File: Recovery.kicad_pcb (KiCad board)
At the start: 2 copper layers, 45 x 37.5 mm, 42 parts, among them J1 DE9_Plug, J2 JST-GH, J3 JST-GH, J4 SWD Header, J5 JST-GH, J6 Micro-Fit, J8 Micro-Fit, U1 STM32F042F6P6TR, U2 AZ1117I-3.3, U3 L7805, U4 MCP2562-E-SN, U5 INA350ABSIDSGR, U6 INA350ABSIDSGR, U8 INA350ABSIDSGR, Y1 8M, ?p

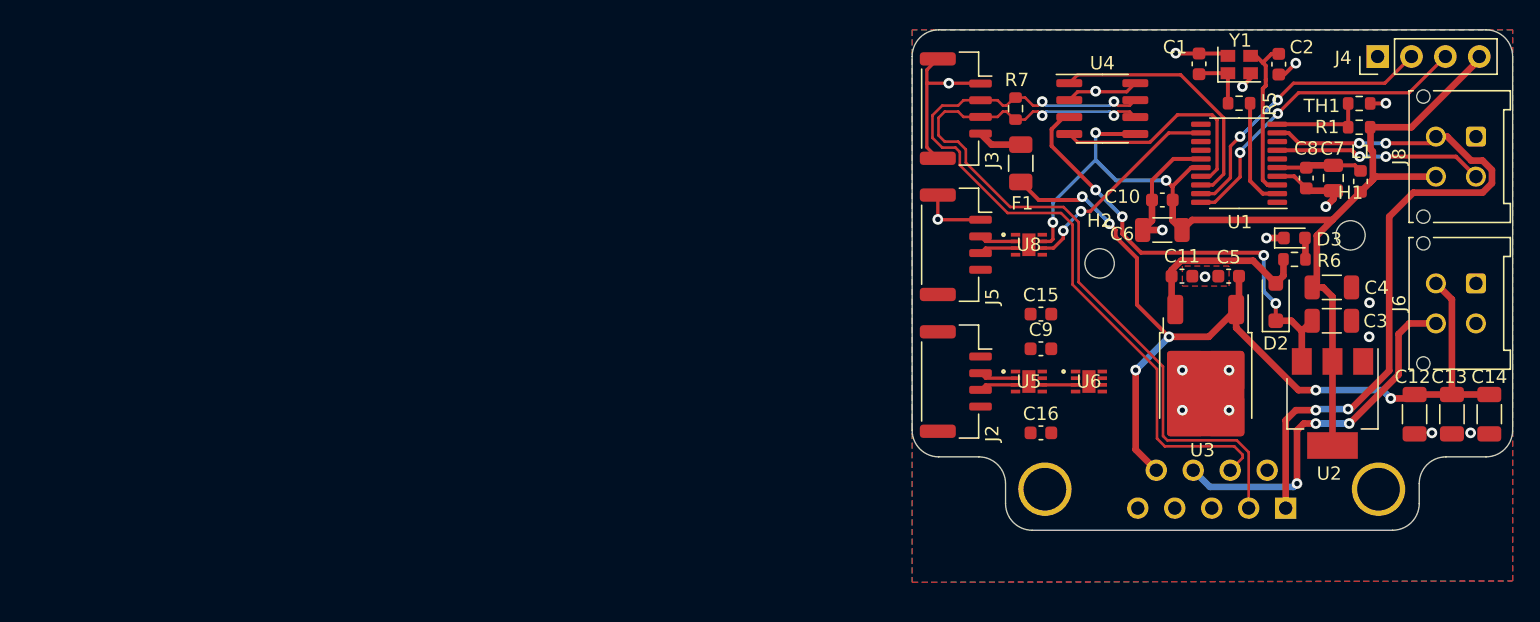
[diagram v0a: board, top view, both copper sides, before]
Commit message: fix pcb size
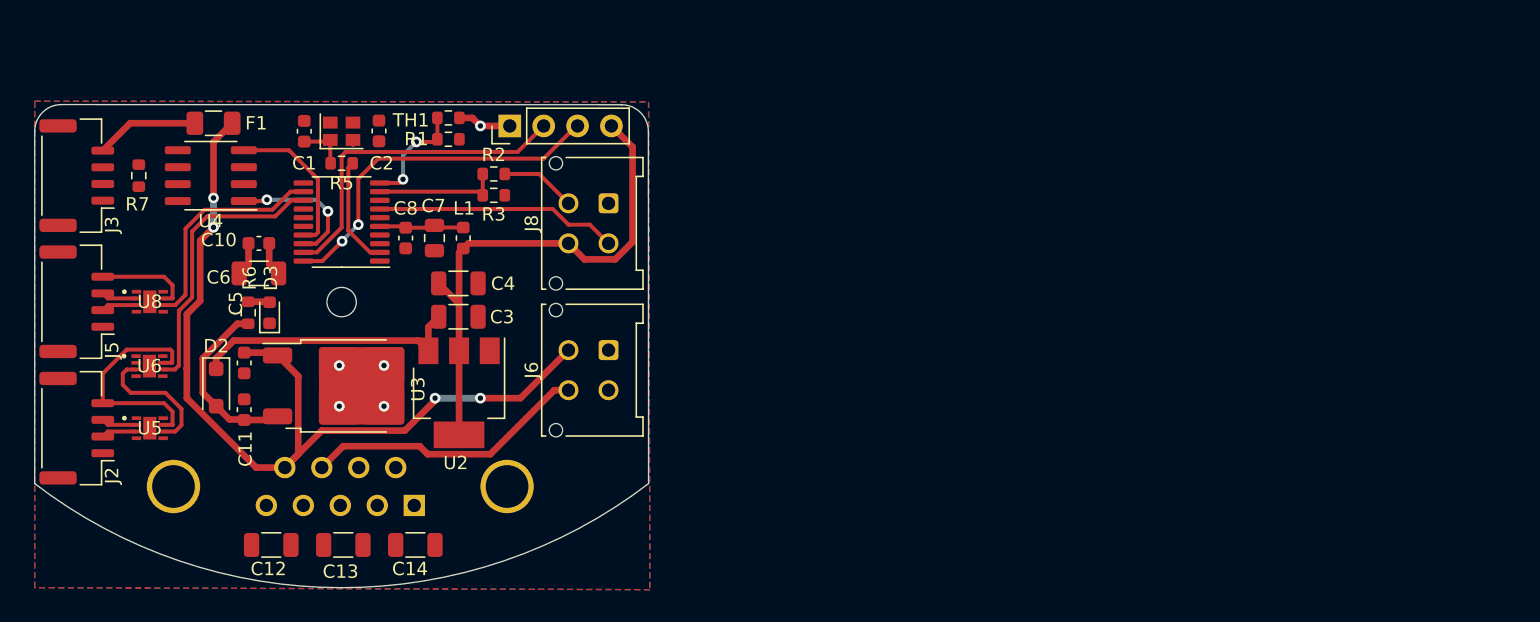
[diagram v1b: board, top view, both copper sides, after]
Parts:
- removed C15, C16, C9: 100n, Capacitor_SMD:C_0603_1608Metric
- removed H2: MountingHole_Pad, MountingHole:MountingHole_2.2mm_M2
- added R2: 1K8, Resistor_SMD:R_0603_1608Metric, F.Cu at (91.4, 86.8)
- added R3: 1K, Resistor_SMD:R_0603_1608Metric, F.Cu at (91.4, 88.4)
- J2, J3, J5: footprint Connector_JST:JST_GH_SM04B-GHS-TB_1x04-1MP_P1.25mm_Horizontal -> Connector_JST:JST_GH_BM04B-GHS-TBT_1x04-1MP_P1.25mm_Vertical
- moved C12 86.2 mm to (74.7, 114.6), turned to 0 degrees
- moved C13 83.7 mm to (80.1, 114.6), turned to 0 degrees
- moved C14 81.1 mm to (85.5, 114.6), turned to 180 degrees
- moved D2 79.7 mm to (70.6, 102.8), turned to -90 degrees
- moved R6 78.5 mm to (73.0, 97.2), turned to 90 degrees
- moved D3 77.0 mm to (74.6, 97.2), turned to 90 degrees
- moved H1 75.8 mm to (80.0, 96.4)
- moved C5 74.1 mm to (72.7, 101.0), turned to 90 degrees
- moved C11 71.0 mm to (72.7, 104.5), turned to -90 degrees
- moved U6 70.4 mm to (65.6, 101.2)
- moved TH1 68.3 mm to (88.0, 82.6)
- moved R1 68.3 mm to (88.0, 84.2)
- moved C10 67.8 mm to (73.8, 92.0)
- moved C6 67.8 mm to (73.8, 94.3)
- moved C8 67.6 mm to (84.8, 91.6)
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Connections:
- U1 pad 9: DEPLOYMENT_SIGNAL -> DEPLOYMENT_PIN
- U5 pad 2: Net-(J2-Pin_2) -> Net-(J2-Pin_3)
- U5 pad 3: Net-(J2-Pin_3) -> Net-(J2-Pin_2)
- U8 pad 2: Net-(J5-Pin_2) -> Net-(J5-Pin_3)
- U8 pad 3: Net-(J5-Pin_3) -> Net-(J5-Pin_2)
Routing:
- net CAN-: track 61.3 -> 0.00 mm, vias 2 -> 0
- net CAN+: track 59.6 -> 0.00 mm, vias 2 -> 0
- net DEPLOYMENT_SIGNAL: track 55.1 -> 5.69 mm, vias 4 -> 0
- net GND: track 48.1 -> 7.44 mm, vias 19 -> 5
- net PRESSURE_SENSOR_1: track 0.00 -> 21.1 mm
- net +3V3: track 80.2 -> 66.2 mm, vias 3 -> 0
- net +5V: track 33.9 -> 20.4 mm, vias 4 -> 0
- net OSC_OUT: track 13.0 -> 0.21 mm
- net DEPLOYMENT_PIN: track 0.00 -> 9.43 mm
- net CAN_TX: track 19.4 -> 10.8 mm, vias 0 -> 2
- net Net-(U5-OUT): track 2.50 -> 9.91 mm
- net +VDC: track 27.9 -> 21.4 mm, vias 3 -> 0
- net CAN_RX: track 17.5 -> 11.6 mm
- net Net-(J3-Pin_4): track 3.36 -> 7.75 mm
- net SWDIO: track 21.5 -> 25.1 mm, vias 2 -> 0
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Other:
- board size 45 x 37.5 mm -> 46 x 36.2 mm

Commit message: finish traces
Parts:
- moved R5 2.86 mm to (77.4, 84.8)
- moved R6 1.41 mm to (74.0, 98.2), turned to 0 degrees
- moved Y1 1.02 mm to (81.0, 83.8)
- moved C2 0.86 mm to (83.6, 83.9)
- moved D3 0.85 mm to (74.0, 96.6), turned to 0 degrees
- moved C1 0.49 mm to (77.4, 83.2), turned to 0 degrees
- moved H1 0.30 mm to (80.0, 96.7)
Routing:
- net +3V3: track 66.2 -> 123.4 mm, vias 0 -> 7
- net CAN-: track 0.00 -> 55.9 mm
- net CAN+: track 0.00 -> 52.1 mm
- net DEPLOYMENT_SIGNAL: track 5.69 -> 40.5 mm, vias 0 -> 1
- net GND: track 7.44 -> 30.0 mm, vias 5 -> 19
- net +5V: track 20.4 -> 38.8 mm, vias 0 -> 2
- net +BATT: track 68.6 -> 86.4 mm, vias 4 -> 6
- net OSC_OUT: track 0.21 -> 11.9 mm
- net CAN_TX: track 10.8 -> 22.0 mm, vias 2 -> 0
- net OSC_IN: track 8.22 -> 10.5 mm
- net Net-(C1-Pad2): track 3.76 -> 4.83 mm
- net TEMPERATURE_SENSOR: track 8.32 -> 7.27 mm, vias 2 -> 0
- net SWCLK: track 26.8 -> 27.7 mm
- net CAN_RX: track 11.6 -> 12.2 mm
- net SWDIO: track 25.1 -> 24.6 mm, vias 0 -> 2

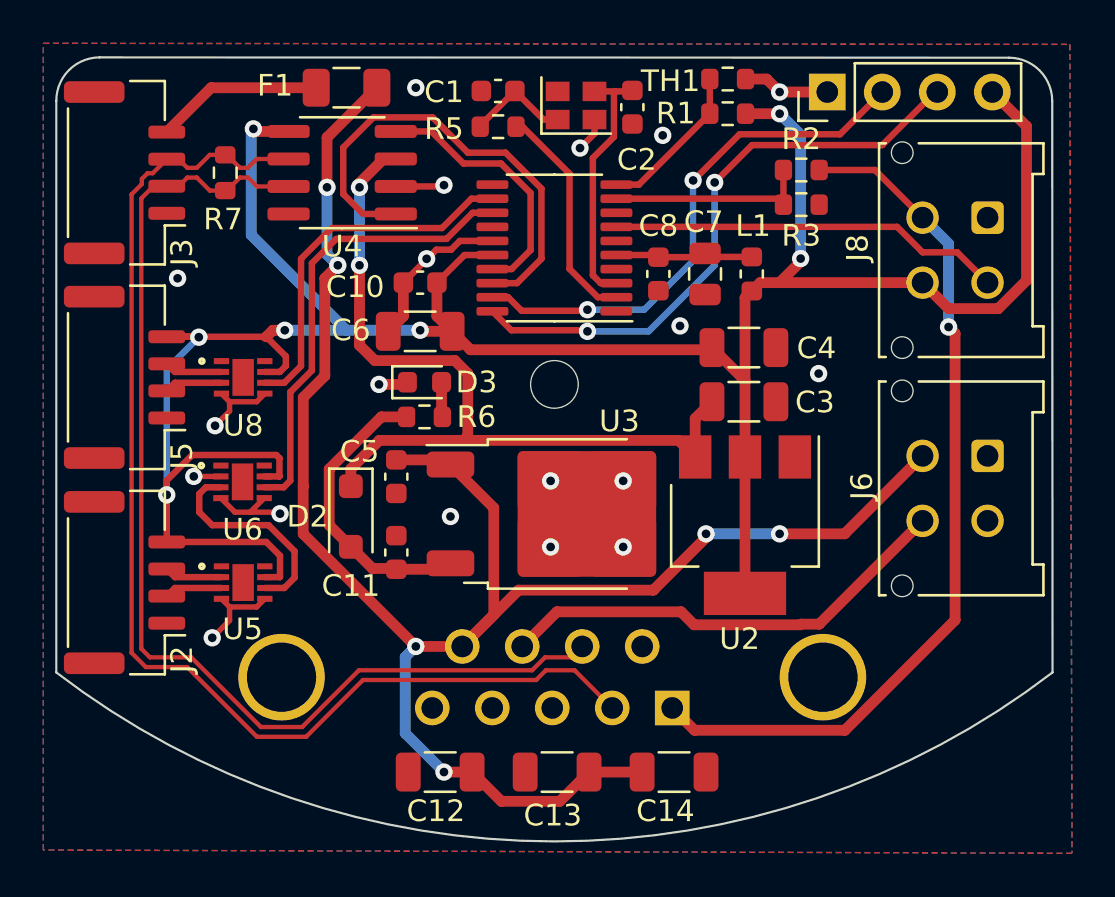
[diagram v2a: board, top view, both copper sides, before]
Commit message: Various small fixes
- increased trace width for deploy signal, removed thermal relief
- left some room around screw, used pad hole type
- tweaked CAN traces
- Added bypass caps to amps, CAN controller
- Removed 5V rail diode & LED, diode used for BAT instead
- Used male D-Sub footprint instead of female (affects pin numbering)
- Added test points for amps
- Pulled BOOT pin low w/ 10k
- Added a jumper to allow differentiating between top and bottom
  recovery
- Add two MCU controllable LEDs
- Added silkscreen (name, rev, logo)
- Added oscillator values
- Added a voltage-divider jumper for one sensor input
- Finished BOM
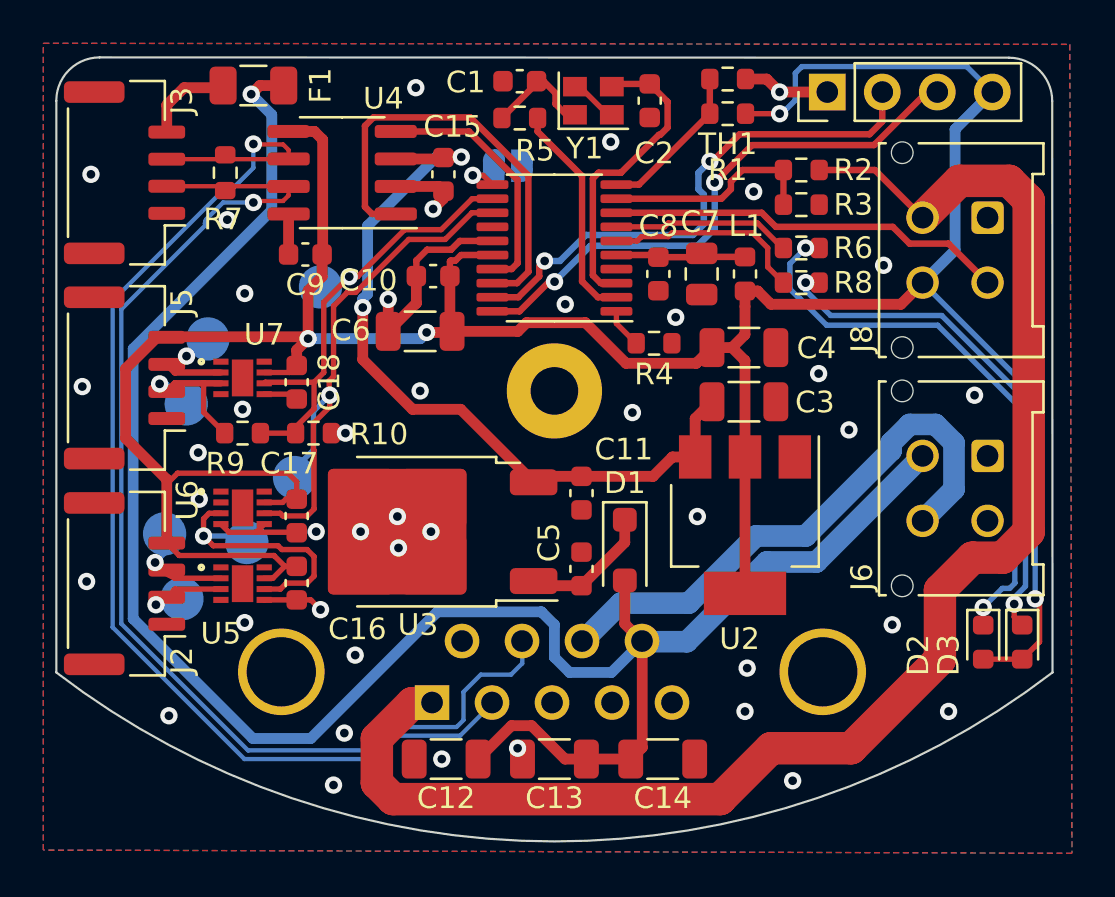
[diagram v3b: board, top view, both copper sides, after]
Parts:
- added C15: 100n, Capacitor_SMD:C_0603_1608Metric, F.Cu at (74.9, 87.0)
- added C16: 100n, Capacitor_SMD:C_0603_1608Metric, F.Cu at (68.1, 105.9)
- added C17: 100n, Capacitor_SMD:C_0603_1608Metric, F.Cu at (68.1, 102.8)
- added C18: 100n, Capacitor_SMD:C_0603_1608Metric, F.Cu at (68.1, 96.6)
- added C9: 100n, Capacitor_SMD:C_0603_1608Metric, F.Cu at (68.5, 90.7)
- added D1: ~, Diode_SMD:D_SOD-123F, F.Cu at (83.2, 104.4)
- added JP1: SolderJumper_2_Open, Jumper:SolderJumper-2_P1.3mm_Open_RoundedPad1.0x1.5mm, B.Cu at (77.8, 86.6)
- added R10: DNP, Resistor_SMD:R_0603_1608Metric, F.Cu at (68.9, 99.0)
- added R4: 10k, Resistor_SMD:R_0603_1608Metric, F.Cu at (84.6, 94.8)
- added R8: 1k, Resistor_SMD:R_0603_1608Metric, F.Cu at (91.4, 92.0)
- added R9: DNP, Resistor_SMD:R_0603_1608Metric, F.Cu at (65.6, 99.0)
- added TP1: TestPoint, TestPoint:TestPoint_Pad_D2.0mm, B.Cu at (62.0, 103.6)
- added TP2: TestPoint, TestPoint:TestPoint_Pad_D2.0mm, B.Cu at (62.8, 106.6)
- added TP3: TestPoint, TestPoint:TestPoint_Pad_D2.0mm, B.Cu at (65.8, 104.0)
- added TP4: TestPoint, TestPoint:TestPoint_Pad_D2.0mm, B.Cu at (68.0, 101.0)
- added TP5: TestPoint, TestPoint:TestPoint_Pad_D2.0mm, B.Cu at (64.0, 94.6)
- added TP6: TestPoint, TestPoint:TestPoint_Pad_D2.0mm, B.Cu at (63.0, 97.6)
- added TP7: TestPoint, TestPoint:TestPoint_Pad_D2.0mm, B.Cu at (69.2, 92.2)
- C1, C2: value 22p -> 10p
- D2: value ~ -> green; footprint Diode_SMD:D_SOD-123F -> LED_SMD:LED_0603_1608Metric
- H1: footprint MountingHole:MountingHole_2.2mm_M2 -> MountingHole:MountingHole_2.2mm_M2_Pad
- J1: footprint Connector_Dsub:DSUB-9_Female_Vertical_P2.77x2.84mm_MountingHoles -> Connector_Dsub:DSUB-9_Male_Vertical_P2.77x2.84mm_MountingHoles
- R1: value 10K -> 10k
- R2: value 1K8 -> 1k8
- R3: value 1K -> 1k
- R5: value 330 -> 1k
- R6: value 220 -> 1k
- TH1: value Thermistor_NTC -> NCU18XH103F6SRB
- Y1: value 8M, ?p -> 8M, 12p
- moved D3 30.1 mm to (101.6, 108.6), turned to -90 degrees
- moved D2 29.8 mm to (99.8, 108.6)
- moved R6 19.1 mm to (91.4, 90.4), turned to 180 degrees
- moved J1 11.1 mm to (74.3, 111.4)
- moved C5 9.55 mm to (81.2, 105.2), turned to -90 degrees
- moved C11 8.98 mm to (81.2, 101.7), turned to 90 degrees
- moved U3 6.29 mm to (74.0, 103.5), turned to 180 degrees
- moved F1 4.30 mm to (66.1, 82.9)
- moved U6 1.20 mm to (65.6, 102.4)
- moved C1 1.10 mm to (78.4, 82.7)
- moved R5 1.08 mm to (78.4, 84.4)
- moved C2 0.85 mm to (84.4, 83.6)
- moved Y1 0.83 mm to (81.8, 83.6)
- moved C14 0.80 mm to (85.0, 114.0)
- moved C10 0.67 mm to (74.4, 91.7)
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- renumbered U8 to U7
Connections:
- C11 pad 2: Net-(D2-A) -> +5V
- C5 pad 2: +BATT -> Net-(D1-K)
- D2 pad 1: +5V -> Net-(D2-K)
- D2 pad 2: Net-(D2-A) -> +3V3
- D3 pad 1: GND -> Net-(D3-K)
- D3 pad 2: Net-(D3-A) -> +3V3
- R6 pad 1: Net-(D2-A) -> Net-(D2-K)
- R6 pad 2: Net-(D3-A) -> LED_GREEN
- U1 pad 1: unconnected-(U1-PB8-Pad1) -> BOOT
- U1 pad 11: unconnected-(U1-PA5-Pad11) -> ADDRESS
- U1 pad 6: unconnected-(U1-PA0-Pad6) -> LED_RED
- U1 pad 7: SERVO_FEEDBACK -> LED_GREEN
- U1 pad 8: unconnected-(U1-PA2-Pad8) -> SERVO_FEEDBACK
- U3 pad 1: +BATT -> Net-(D1-K)
- U3 pad 3: Net-(D2-A) -> +5V
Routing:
- net DEPLOYMENT_SIGNAL: track 40.5 -> 69.6 mm, vias 1 -> 0
- net Net-(D2-K): track 0.00 -> 26.5 mm, vias 0 -> 2
- net Net-(D3-K): track 0.00 -> 24.0 mm, vias 0 -> 2
- net +3V3: track 123.4 -> 146.3 mm, vias 7 -> 4
- net Net-(D2-A): track 13.7 -> 0.00 mm
- net LED_RED: track 0.00 -> 9.33 mm
- net LED_GREEN: track 0.00 -> 8.26 mm
- net +BATT: track 86.4 -> 93.4 mm, vias 6 -> 1
- net Net-(D1-K): track 0.00 -> 6.17 mm
- net Net-(J5-Pin_2): track 2.68 -> 7.82 mm, vias 0 -> 1
- net PRESSURE_SENSOR_2: track 16.9 -> 21.8 mm, vias 0 -> 1
- net PRESSURE_SENSOR_1: track 21.1 -> 25.9 mm, vias 0 -> 1
- net +VDC: track 21.4 -> 26.1 mm
- net Net-(J3-Pin_4): track 7.75 -> 4.22 mm
- net Net-(J2-Pin_3): track 2.68 -> 5.80 mm, vias 0 -> 1
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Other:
- board text added: "FRODO Recovery"
- board text added: "JLCJLCJLCJLC"
- board text added: "rev 1"
